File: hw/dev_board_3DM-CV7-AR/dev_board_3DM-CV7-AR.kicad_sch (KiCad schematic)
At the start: 11 parts

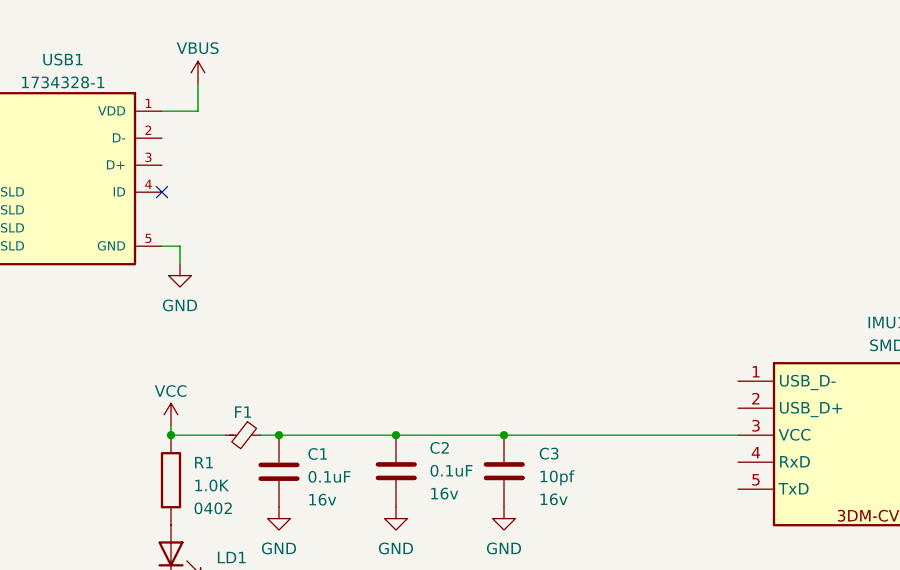
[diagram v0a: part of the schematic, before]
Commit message: Añadido CM Choke
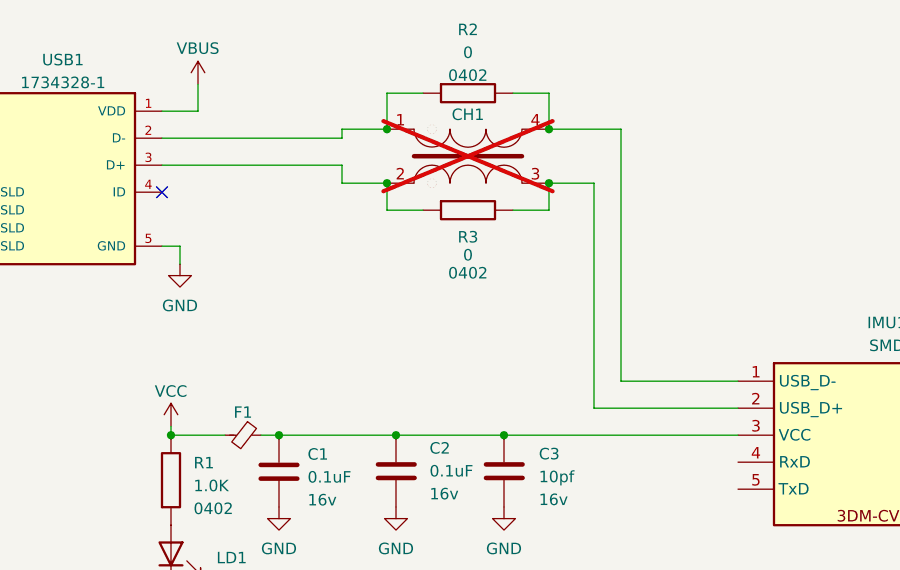
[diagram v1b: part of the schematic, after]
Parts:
- added CH1: ~, Herranz - Filtering:XFMR_CM0805D900R-10, symbol Herranz - Filtering:CMC_CM0805D900R-10
- added R2, R3: 0, Resistor_SMD:R_0402_1005Metric, symbol Herranz - Resistors (0402):0
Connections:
- net at IMU1.1 (USB_D-): now also CH1.4, R2.2
- net at IMU1.2 (USB_D+): now also CH1.3, R3.2
- net at USB1.2 (D-): now also CH1.1, R2.1
- net at USB1.3 (D+): now also CH1.2, R3.1
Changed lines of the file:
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@@
 (kicad_sch (version 20230121) (generator eeschema)
   (paper "A4")
+  (junction (at 103 75) (diameter 0) (color 0 0 0 0)
+  )
   (junction (at 73 109) (diameter 0) (color 0 0 0 0)
   )
   (junction (at 36 86) (diameter 0) (color 0 0 0 0)
   )
+  (junction (at 103 81) (diameter 0) (color 0 0 0 0)
+  )
   (junction (at 36 84) (diameter 0) (color 0 0 0 0)
   )
+  (junction (at 85 75) (diameter 0) (color 0 0 0 0)
+  )
   (junction (at 98 109) (diameter 0) (color 0 0 0 0)
   )
@@
   )
   (junction (at 61 109) (diameter 0) (color 0 0 0 0)
+  )
+  (junction (at 85 81) (diameter 0) (color 0 0 0 0)
   )
   (no_connect (at 154 103))
@@
     (stroke (width 0) (type default))
   )
+  (wire (pts (xy 99 84) (xy 103 84))
+    (stroke (width 0) (type default))
+  )
   (wire (pts (xy 36 86) (xy 36 88))
     (stroke (width 0) (type default))
@@
     (stroke (width 0) (type default))
   )
+  (wire (pts (xy 89 84) (xy 85 84))
+    (stroke (width 0) (type default))
+  )
   (wire (pts (xy 38 82) (xy 36 82))
     (stroke (width 0) (type default))
   )
+  (wire (pts (xy 80 75) (xy 80 76))
+    (stroke (width 0) (type default))
+  )
+  (wire (pts (xy 103 84) (xy 103 81))
+    (stroke (width 0) (type default))
+  )
   (wire (pts (xy 60 73) (xy 64 73))
     (stroke (width 0) (type default))
   )
+  (wire (pts (xy 60 79) (xy 80 79))
+    (stroke (width 0) (type default))
+  )
+  (wire (pts (xy 80 75) (xy 85 75))
+    (stroke (width 0) (type default))
+  )
   (wire (pts (xy 36 82) (xy 36 84))
     (stroke (width 0) (type default))
   )
+  (wire (pts (xy 99 71) (xy 103 71))
+    (stroke (width 0) (type default))
+  )
   (wire (pts (xy 61 109) (xy 67 109))
     (stroke (width 0) (type default))
   )
+  (wire (pts (xy 80 79) (xy 80 81))
+    (stroke (width 0) (type default))
+  )
   (wire (pts (xy 36 84) (xy 36 86))
     (stroke (width 0) (type default))
@@
     (stroke (width 0) (type default))
   )
+  (wire (pts (xy 103 75) (xy 111 75))
+    (stroke (width 0) (type default))
+  )
+  (wire (pts (xy 85 71) (xy 85 75))
+    (stroke (width 0) (type default))
+  )
+  (wire (pts (xy 108 81) (xy 108 106))
+    (stroke (width 0) (type default))
+  )
+  (wire (pts (xy 85 84) (xy 85 81))
+    (stroke (width 0) (type default))
+  )
+  (wire (pts (xy 111 103) (xy 124 103))
+    (stroke (width 0) (type default))
+  )
   (wire (pts (xy 64 73) (xy 64 70))
     (stroke (width 0) (type default))
   )
+  (wire (pts (xy 103 71) (xy 103 75))
+    (stroke (width 0) (type default))
+  )
   (wire (pts (xy 36 86) (xy 38 86))
     (stroke (width 0) (type default))
   )
+  (wire (pts (xy 108 106) (xy 124 106))
+    (stroke (width 0) (type default))
+  )
   (wire (pts (xy 73 109) (xy 86 109))
     (stroke (width 0) (type default))
   )
+  (wire (pts (xy 89 71) (xy 85 71))
+    (stroke (width 0) (type default))
+  )
+  (wire (pts (xy 60 76) (xy 80 76))
+    (stroke (width 0) (type default))
+  )
+  (wire (pts (xy 80 81) (xy 85 81))
+    (stroke (width 0) (type default))
+  )
   (wire (pts (xy 71 109) (xy 73 109))
     (stroke (width 0) (type default))
@@
     (stroke (width 0) (type default))
   )
+  (wire (pts (xy 103 81) (xy 108 81))
+    (stroke (width 0) (type default))
+  )
   (wire (pts (xy 154 109) (xy 161 109))
     (stroke (width 0) (type default))
@@
   )
   (wire (pts (xy 38 88) (xy 36 88))
+    (stroke (width 0) (type default))
+  )
+  (wire (pts (xy 111 75) (xy 111 103))
     (stroke (width 0) (type default))
   )
@@
     )
   )
+  (symbol (lib_id "Herranz - Resistors (0402):0") (at 94 83 0) (unit 1)
+    (in_bom yes) (on_board yes) (dnp no)
+    (property "Reference" "R3" (at 94 87 0)
+      (effects (font (size 1.27 1.27)))
+    )
+    (property "Value" "0" (at 94 89 0)
+      (effects (font (size 1.27 1.27)))
+    )
+    (property "Footprint" "Resistor_SMD:R_0402_1005Metric" (at 94 80 0)
+      (effects (font (size 1.27 1.27)) hide)
+    )
+    (property "Datasheet" "" (at 94 83 0)
+      (effects (font (size 1.27 1.27)) hide)
+    )
+    (property "Size" "0402" (at 94 91 0)
+      (effects (font (size 1.27 1.27)))
+    )
+    (pin "1")
+    (pin "2")
+    (instances
+      (project "dev_board_3DM-CV7-AR"
+        (path "/e067fbf5-07c4-4cb2-9229-7d163502827d"
+          (reference "R3") (unit 1)
+        )
+      )
+    )
+  )
   (symbol (lib_id "Herranz - Capacitor (0402):Gen_C") (at 98 107 0) (unit 1)
     (in_bom yes) (on_board yes) (dnp no) (fields_autoplaced)
@@
         (path "/e067fbf5-07c4-4cb2-9229-7d163502827d"
           (reference "#PWR04") (unit 1)
+        )
+      )
+    )
+  )
+  (symbol (lib_id "Herranz - Filtering:CMC_CM0805D900R-10") (at 94 73 0) (unit 1)
+    (in_bom yes) (on_board yes) (dnp yes) (fields_autoplaced)
+    (property "Reference" "CH1" (at 94 73.39 0)
+      (effects (font (size 1.27 1.27)))
+    )
+    (property "Value" "~" (at 94 73 0)
+      (effects (font (size 1.27 1.27)))
+    )
+    (property "Footprint" "Herranz - Filtering:XFMR_CM0805D900R-10" (at 94 84 0)
+      (effects (font (size 1.27 1.27)) hide)
+    )
+    (property "Datasheet" "" (at 94 73 0)
+      (effects (font (size 1.27 1.27)) hide)
+    )
+    (pin "1")
+    (pin "2")
+    (pin "3")
+    (pin "4")
+    (instances
+      (project "dev_board_3DM-CV7-AR"
+        (path "/e067fbf5-07c4-4cb2-9229-7d163502827d"
+          (reference "CH1") (unit 1)
         )
       )
@@
         )
       )
+    )
+  )
+  (symbol (lib_id "Herranz - Resistors (0402):0") (at 94 70 0) (unit 1)
+    (in_bom yes) (on_board yes) (dnp no) (fields_autoplaced)
+    (property "Reference" "R2" (at 94 63.96 0)
+      (effects (font (size 1.27 1.27)))
+    )
+    (property "Value" "0" (at 94 66.5 0)
+      (effects (font (size 1.27 1.27)))
+    )
+    (property "Footprint" "Resistor_SMD:R_0402_1005Metric" (at 94 67 0)
+      (effects (font (size 1.27 1.27)) hide)
+    )
+    (property "Datasheet" "" (at 94 70 0)
+      (effects (font (size 1.27 1.27)) hide)
+    )
+    (property "Size" "0402" (at 94 69.04 0)
+      (effects (font (size 1.27 1.27)))
+    )
+    (pin "1")
+    (pin "2")
+    (instances
+      (project "dev_board_3DM-CV7-AR"
+        (path "/e067fbf5-07c4-4cb2-9229-7d163502827d"
+          (reference "R2") (unit 1)
+        )
+      )

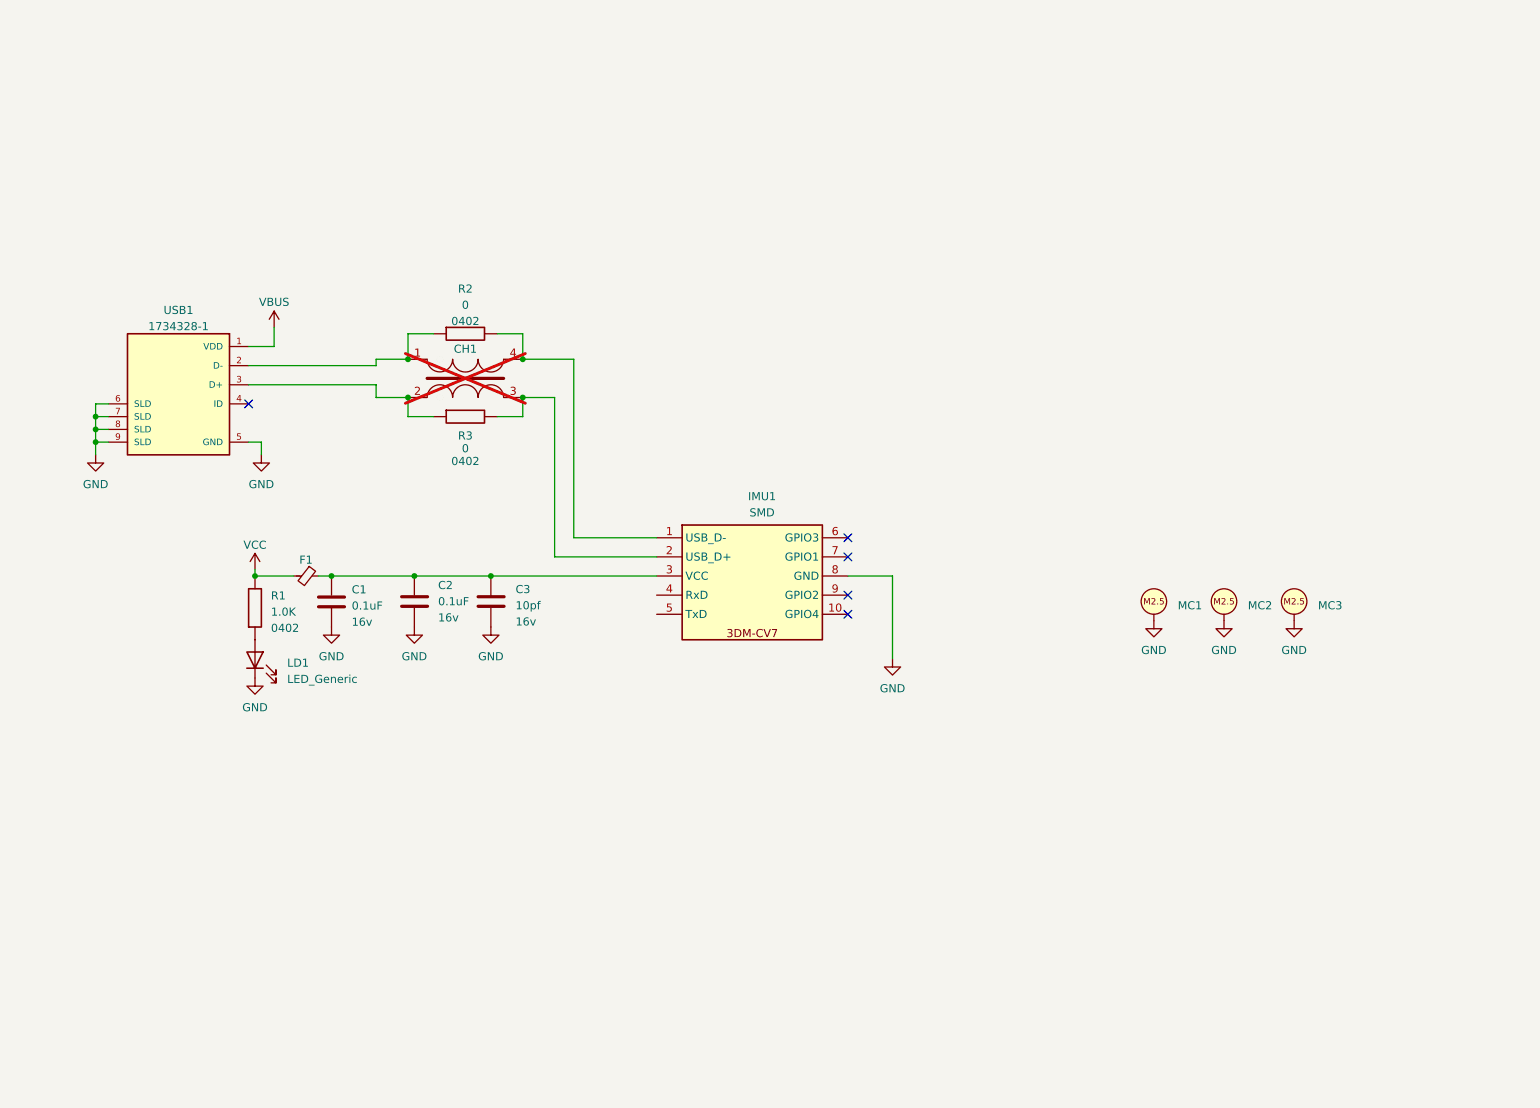
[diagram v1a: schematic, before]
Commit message: Añadido Leds TX-RX
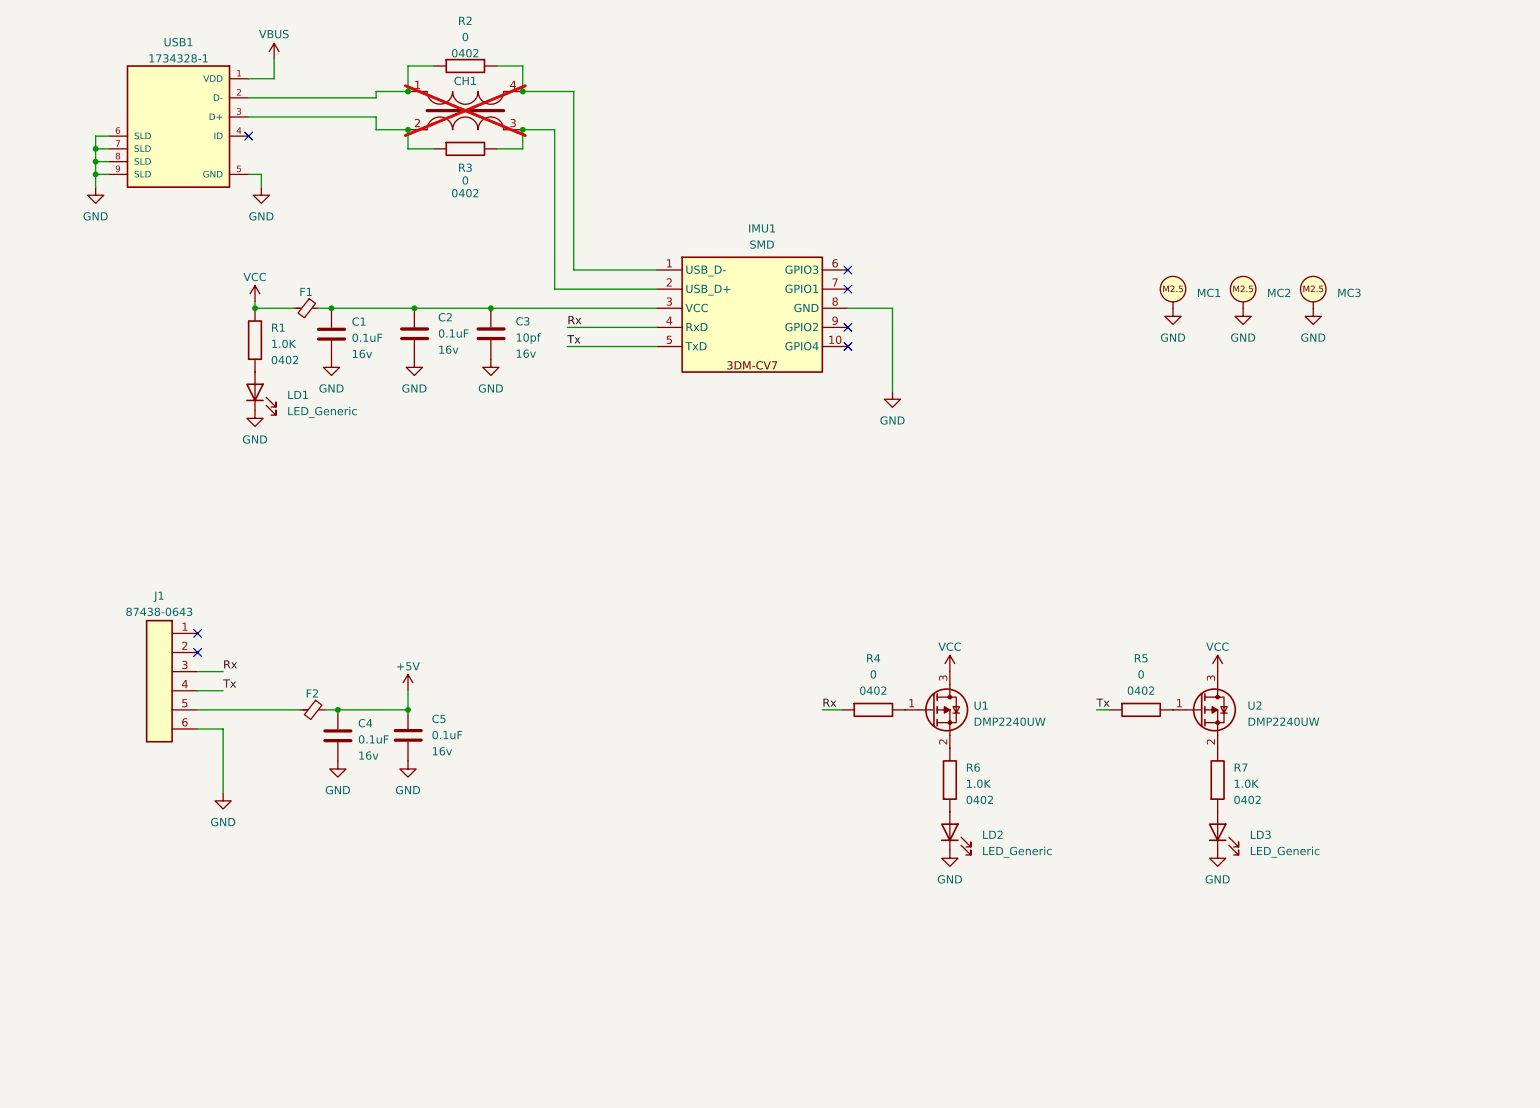
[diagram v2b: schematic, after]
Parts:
- added C4: 0.1uF, Capacitor_SMD:C_0805_2012Metric, symbol Herranz - Capacitor (0805):Gen_C
- added C5: 0.1uF, Capacitor_SMD:C_0402_1005Metric, symbol Herranz - Capacitor (0402):Gen_C
- added F2: ~, Inductor_SMD:L_0402_1005Metric_Pad0.77x0.64mm_HandSolder, symbol Herranz - Ferrite:Gen_F
- added J1: 87438-0643, Herranz - Conn Molex:Molex_picoSPOX_87438-3.5A_1x6_P1.5mm_Horizontal, symbol Herranz - Conn Molex:Molex_picoSPOX_87438-3.5A_1x6_P1.5mm_Horizontal
- added LD2, LD3: LED_Generic, LED_SMD:LED_0402_1005Metric_Pad0.77x0.64mm_HandSolder, symbol Herranz - LED:LED_Generic
- added R4, R5: 0, Resistor_SMD:R_0402_1005Metric, symbol Herranz - Resistors (0402):0
- added R6, R7: 1.0K, Resistor_SMD:R_0402_1005Metric, symbol Herranz - Resistors (0402):1.0K
- added U1, U2: DMP2240UW, Package_TO_SOT_SMD:SOT-323_SC-70, symbol Herranz - Transistor:DMP2240UW-7
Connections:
- net +3V3: now also U1.3 (D), U2.3 (D)
- net GND: now also C4.2, C5.2, J1.6 (Pin_6), LD2.2 (K), LD3.2 (K)
- net Rx: now reaches IMU1.4 (RxD)
- net Rx: now also J1.3 (Pin_3), R4.1
- net Tx: now reaches IMU1.5 (TxD)
- net Tx: now also J1.4 (Pin_4), R5.1
- new net: R4.2, U1.1 (G)
- new net: R6.2, U1.2 (S)
- new net: F2.1, J1.5 (Pin_5)
- new net: R5.2, U2.1 (G)
- new net: R7.2, U2.2 (S)
- new net: LD3.1 (A), R7.1
- new net: LD2.1 (A), R6.1
- new net +5V: C4.1, C5.1, F2.2
- no-connect marks 5 -> 7
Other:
- moved on the sheet: C1, C2, C3, CH1, F1, IMU1, LD1, MC1, MC2, MC3, R1, R2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

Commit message: arreglado linea diferencial
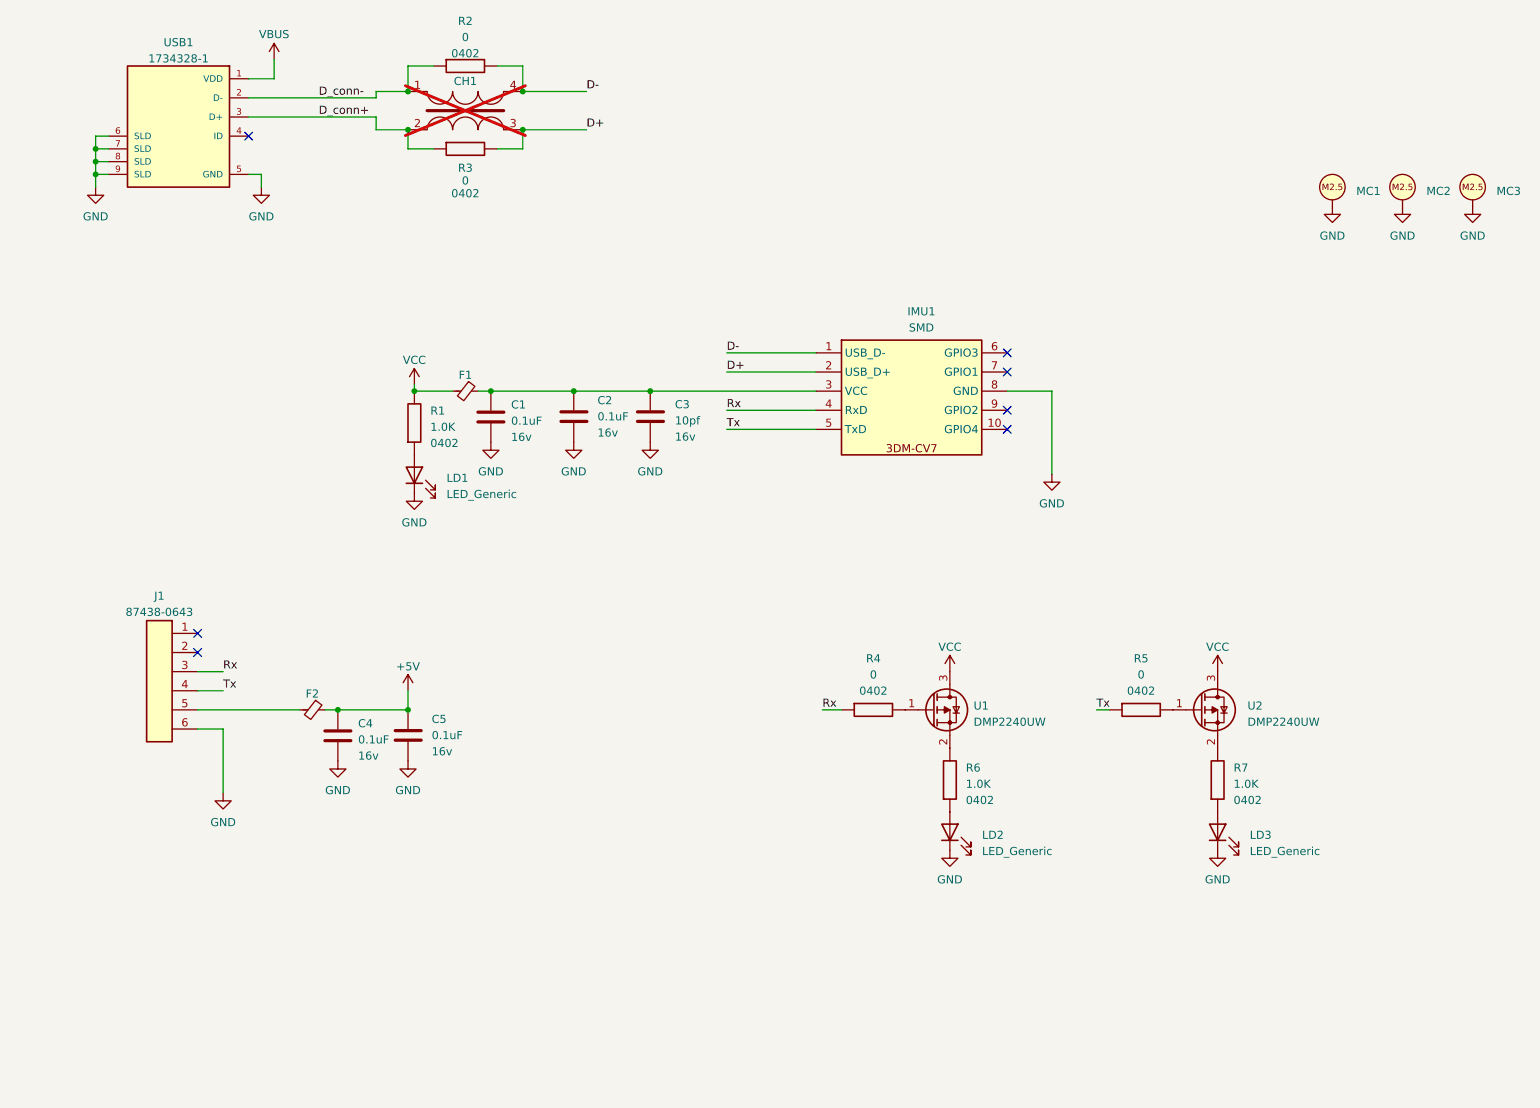
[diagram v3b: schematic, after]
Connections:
- net D-: now reaches CH1.4, IMU1.1 (USB_D-), R2.2
- net D+: now reaches CH1.3, IMU1.2 (USB_D+), R3.2
- net D_conn+: now reaches CH1.2, R3.1, USB1.3 (D+)
- net D_conn-: now reaches CH1.1, R2.1, USB1.2 (D-)
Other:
- moved on the sheet: C1, C2, C3, F1, IMU1, LD1, MC1, MC2, MC3, R1

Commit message: Finalizado
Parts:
- added MC4, MC5, MC6: M3_Hole, Herranz - Various:M3_Hole, symbol Herranz - Various:M3_Hole
- added SEL1: ~, Herranz - Various:pad_selector, symbol Herranz - Various:SEL_PAD
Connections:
- net +5V: now also SEL1.1
- net GND: now also MC4.1, MC5.1, MC6.1; no longer MC3.1
- net VBUS: now also SEL1.2
- net at R6.2: now also U1.3 (D); no longer U1.2 (S)
- net at R7.2: now also U2.3 (D); no longer U2.2 (S)
- net +3V3 renamed +5VD
- net +5VD: now also U1.2 (S), U2.2 (S), SEL1.3; no longer U1.3 (D), U2.3 (D)
- no-connect marks 7 -> 8
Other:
- note added: "Designer: Borja Herranz"
- note added: "Dev Board 3DM-CV7"
- note added: "Drops inside the forbidden magnetic zone"
- note added: "MOTUS"
- note added: "Parker 3DM-CV7"
- note added: "Rx LED"
- note added: "Serial TTL Connection"
- note added: "Tx LED"
- note added: "USB Connection"
- note added: "Voltage Selector for USB or MotusIMU Board"
- moved on the sheet: C1, C2, C3, C4, C5, CH1, F1, F2, IMU1, J1, LD1, LD2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
